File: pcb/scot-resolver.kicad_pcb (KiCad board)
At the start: 2 copper layers, 158 parts, among them IC1 AD8692ARMZ, IC10 AD2S1210, IC2 AD8397ARZ, IC3 AD8692ARMZ, IC4 TSR1, IC5 AD8692ARMZ, IC6 AD8692ARMZ, IC7 AD8692ARMZ, IC8 MCP2562, IC9 STM32F0xxKxTx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

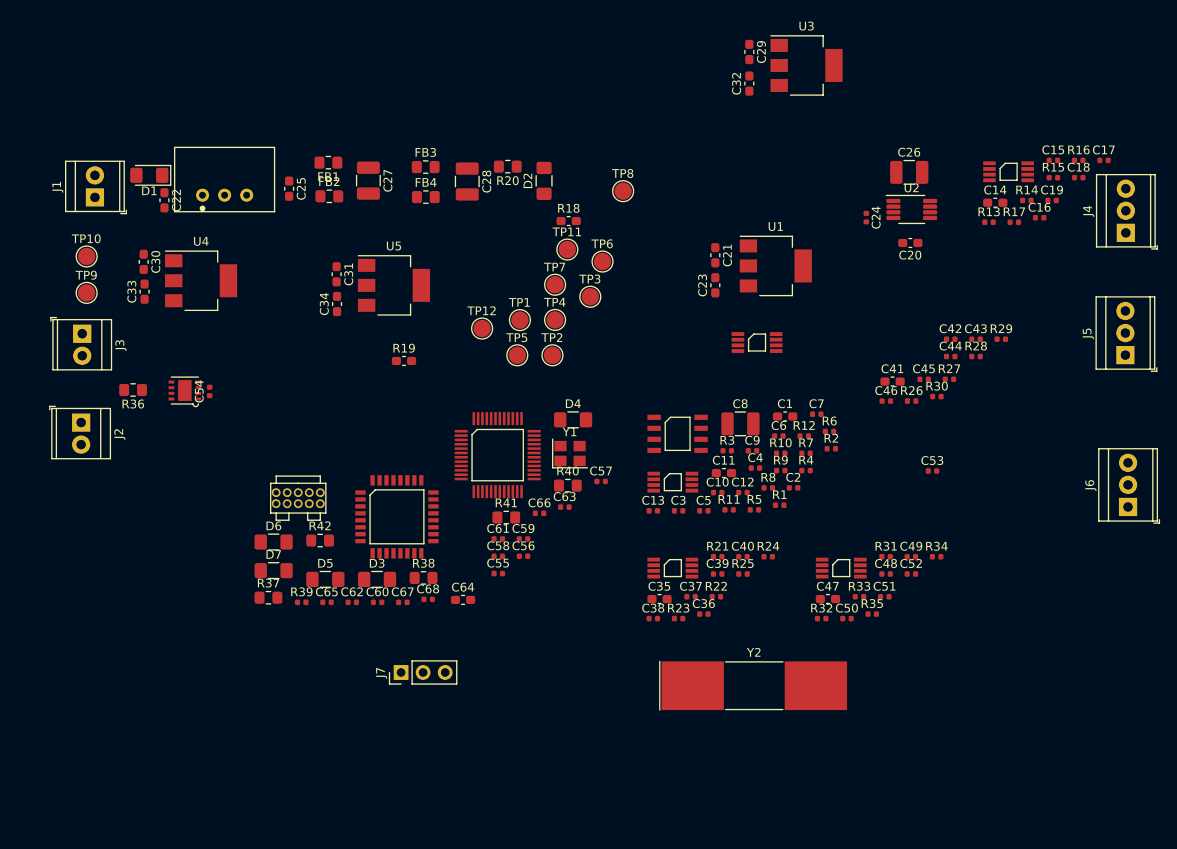
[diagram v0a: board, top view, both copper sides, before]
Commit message: PCB Progress, laying tracks.
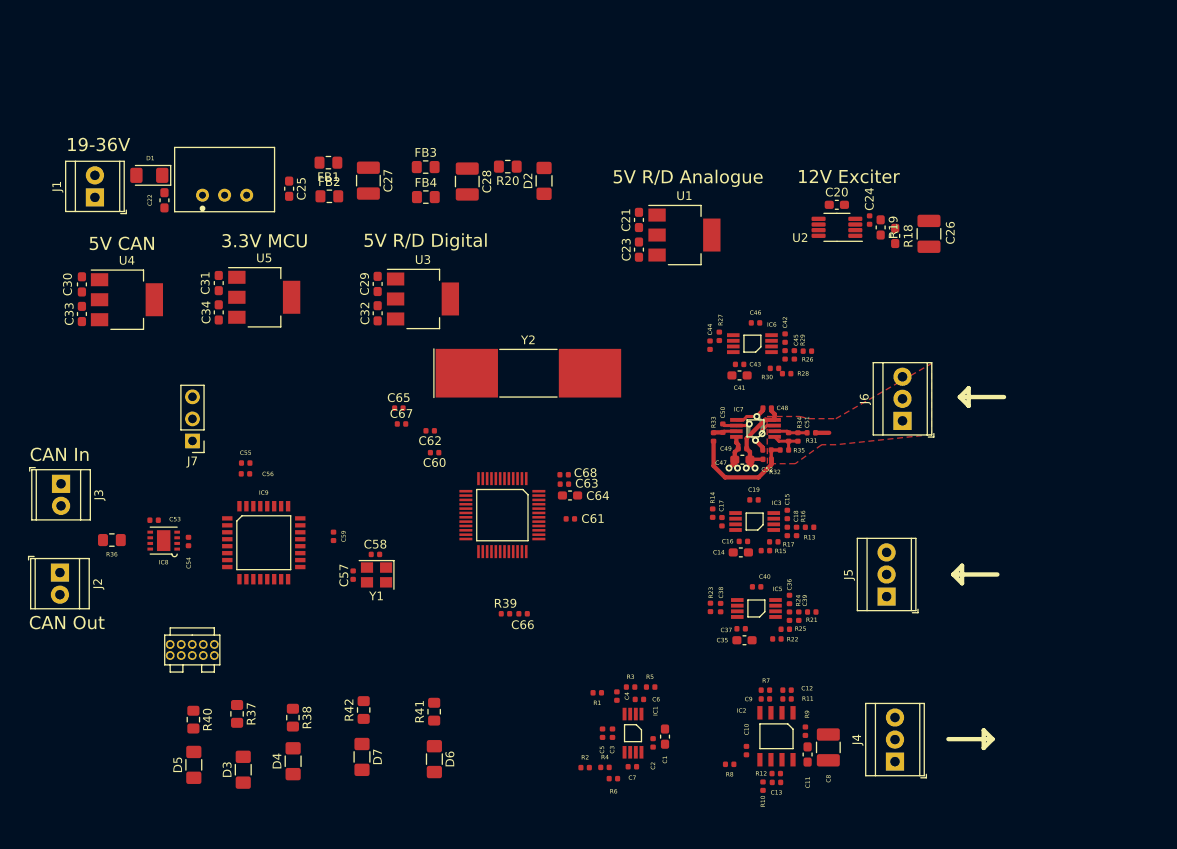
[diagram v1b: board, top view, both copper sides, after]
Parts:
- removed TP1, TP10, TP11, TP12, TP2, TP3, TP4, TP5, TP6, TP7, TP8, TP9: TestPoint, TestPoint:TestPoint_Pad_D2.0mm
- moved C53 89.8 mm to (92.8, 97.5), turned to 180 degrees
- moved J4 66.4 mm to (178.1, 125.3)
- moved C17 60.5 mm to (158.1, 97.7), turned to 270 degrees
- moved R19 57.0 mm to (176.4, 63.8), turned to 90 degrees
- moved R15 54.2 mm to (163.1, 101.0)
- moved R16 53.6 mm to (166.7, 98.8), turned to 270 degrees
- moved C18 52.7 mm to (165.7, 98.8), turned to 270 degrees
- moved U3 51.7 mm to (123.7, 72.1)
- moved R14 51.0 mm to (157.1, 96.7), turned to 90 degrees
- moved C15 51.0 mm to (165.7, 96.9), turned to 270 degrees
- moved R40 50.8 mm to (97.3, 120.5), turned to 270 degrees
- moved D4 50.8 mm to (108.8, 125.3), turned to 90 degrees
- moved C16 50.5 mm to (160.6, 100.0), turned to 180 degrees
- moved C29 50.4 mm to (118.5, 70.3)
- moved C32 50.3 mm to (118.5, 73.7)
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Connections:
- C12 pad 2: /Resolver Exciter/EXC+_OUTPUT -> /Resolver Exciter/EXC-_OUTPUT
- C13 pad 1: /Resolver Exciter/EXC-_OUTPUT -> /Resolver Exciter/EXC+_OUTPUT
- IC2 pad 1: /Resolver Exciter/EXC+_OUTPUT -> /Resolver Exciter/EXC-_OUTPUT
- IC2 pad 7: /Resolver Exciter/EXC-_OUTPUT -> /Resolver Exciter/EXC+_OUTPUT
- J4 pad 2: /Resolver Exciter/EXC-_OUTPUT -> /Resolver Exciter/EXC+_OUTPUT
- J4 pad 3: /Resolver Exciter/EXC+_OUTPUT -> /Resolver Exciter/EXC-_OUTPUT
- R1 pad 2: /Resolver Exciter/AD2S1210_EXC+ -> /Resolver Exciter/AD2S1210_EXC-
- R11 pad 2: /Resolver Exciter/EXC+_OUTPUT -> /Resolver Exciter/EXC-_OUTPUT
- R12 pad 1: /Resolver Exciter/EXC-_OUTPUT -> /Resolver Exciter/EXC+_OUTPUT
- R2 pad 1: /Resolver Exciter/AD2S1210_EXC- -> /Resolver Exciter/AD2S1210_EXC+
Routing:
- net Net-(C52-Pad1): track 0.00 -> 13.4 mm
- net GNDA: track 0.00 -> 12.1 mm, vias 0 -> 2
- net /Resolver Exciter/AD2S1210_VREF: track 0.00 -> 8.05 mm, vias 0 -> 2
- net Net-(C50-Pad1): track 0.00 -> 6.84 mm, vias 0 -> 2
- net /Microcontroller & Interface/5V_RESOLVER_ANALOGUE: track 0.00 -> 5.20 mm, vias 0 -> 2
- net Net-(C51-Pad2): track 0.00 -> 3.95 mm
- net Net-(C51-Pad1): track 0.00 -> 3.81 mm
- net /Resolver Receiver COS-/AD2S1210_INPUT: track 0.00 -> 2.70 mm
- net /Resolver Receiver COS-/RECEIVER_INPUT: track 0.00 -> 1.57 mm
- added copper zone on F.Cu, net GNDA
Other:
- board text added: "12V Exciter"
- board text added: "19-36V"
- board text added: "3.3V MCU"
- board text added: "5V CAN"
- board text added: "5V R/D Analogue"
- board text added: "5V R/D Digital"
- board text added: "CAN In"
- board text added: "CAN Out"

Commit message: Progress.
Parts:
- moved R28 9.07 mm to (156.8, 78.3), turned to 270 degrees
- moved R27 6.03 mm to (162.9, 79.6), turned to 0 degrees
- moved C46 5.90 mm to (163.0, 80.6), turned to 180 degrees
- moved C42 2.95 mm to (163.0, 74.8), turned to 180 degrees
- moved C44 1.10 mm to (157.9, 77.2)
- moved R30 0.88 mm to (164.9, 79.6), turned to 0 degrees
- moved C45 0.38 mm to (165.4, 78.1)
- moved R26 0.38 mm to (168.0, 77.7)
- moved R29 0.38 mm to (166.5, 78.1)
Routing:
- net Net-(C46-Pad1): track 0.00 -> 14.0 mm
- net GNDA: track 12.1 -> 24.7 mm, vias 2 -> 4
- net Net-(C44-Pad1): track 0.00 -> 6.55 mm, vias 0 -> 2
- net /Microcontroller & Interface/5V_RESOLVER_ANALOGUE: track 5.20 -> 10.9 mm, vias 2 -> 4
- net Net-(C45-Pad2): track 0.00 -> 3.83 mm
- net Net-(C45-Pad1): track 0.00 -> 3.71 mm
- net /Resolver Receiver COS+/AD2S1210_INPUT: track 0.00 -> 2.70 mm
- net /Resolver Exciter/AD2S1210_VREF: track 8.05 -> 9.92 mm, vias 2 -> 3

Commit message: Progress.
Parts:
- moved R14 7.09 mm to (163.3, 100.1), turned to 0 degrees
- moved R15 6.50 mm to (157.1, 98.7), turned to 270 degrees
- moved C19 6.09 mm to (163.3, 101.1), turned to 180 degrees
- moved C40 6.07 mm to (163.5, 111.1), turned to 180 degrees
- moved R10 5.50 mm to (161.0, 123.0), turned to 90 degrees
- moved C15 2.86 mm to (163.2, 95.4), turned to 180 degrees
- moved C36 2.78 mm to (163.4, 105.4), turned to 180 degrees
- moved R22 1.51 mm to (163.4, 110.1)
- moved R23 1.26 mm to (157.4, 108.7), turned to 270 degrees
- moved R17 1.14 mm to (165.2, 100.1)
- moved C10 0.94 mm to (160.0, 124.1)
- moved C1 0.75 mm to (151.5, 123.2)
- moved R8 0.49 mm to (159.5, 125.6)
- moved C37 0.46 mm to (160.8, 110.0)
- moved C38 0.40 mm to (158.4, 107.7)
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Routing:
- net GNDA: track 24.7 -> 50.3 mm
- net /Resolver Exciter/AD2S1210_VREF: track 9.92 -> 32.7 mm, vias 3 -> 8
- net Net-(C38-Pad1): track 0.00 -> 7.02 mm, vias 0 -> 2
- net Net-(C17-Pad1): track 0.00 -> 6.79 mm, vias 0 -> 2
- net Net-(C12-Pad1): track 0.00 -> 6.76 mm
- net Net-(C13-Pad2): track 0.00 -> 6.46 mm
- net /Microcontroller & Interface/5V_RESOLVER_ANALOGUE: track 10.9 -> 16.9 mm
- net /Power Supplies/12V_EXCITER: track 0.00 -> 4.26 mm
- net Net-(C39-Pad2): track 0.00 -> 3.93 mm
- net Net-(C18-Pad2): track 0.00 -> 3.84 mm
- net Net-(C10-Pad2): track 0.00 -> 3.74 mm
- net Net-(C39-Pad1): track 0.00 -> 3.71 mm
- net Net-(C18-Pad1): track 0.00 -> 3.67 mm
- net /Resolver Exciter/EXC-_OUTPUT: track 0.00 -> 2.69 mm
- net /Resolver Exciter/EXC+_OUTPUT: track 0.00 -> 2.69 mm
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
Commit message: Progress.
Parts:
- moved D3 20.5 mm to (123.4, 124.6)
- moved D4 20.3 mm to (129.1, 124.3)
- moved D5 20.3 mm to (117.7, 124.7)
- moved R37 20.3 mm to (122.7, 118.8)
- moved R38 20.3 mm to (129.1, 119.2)
- moved R40 20.3 mm to (117.6, 119.5)
- moved D6 16.4 mm to (108.7, 125.3)
- moved R42 16.4 mm to (100.5, 119.6)
- moved D7 16.4 mm to (100.3, 125.0)
- moved R41 16.4 mm to (108.6, 119.8)
- moved C27 3.23 mm to (115.4, 60.9)
- moved FB2 2.50 mm to (111.7, 62.4)
- moved C5 2.25 mm to (144.5, 124.3)
- moved R1 1.85 mm to (145.6, 117.2)
- moved R2 1.60 mm to (144.0, 125.8)
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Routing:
- net /Power Supplies/POWER_28V-: track 0.00 -> 26.9 mm
- net GNDA: track 50.3 -> 69.4 mm, vias 4 -> 8
- net Net-(C40-Pad1): track 2.08 -> 14.0 mm
- net Net-(C19-Pad1): track 1.98 -> 13.5 mm
- net Net-(C25-Pad1): track 0.00 -> 8.46 mm
- net /Microcontroller & Interface/5V_RESOLVER_ANALOGUE: track 16.9 -> 25.3 mm, vias 4 -> 8
- net Net-(C22-Pad1): track 0.00 -> 7.52 mm
- net /Resolver Exciter/AD2S1210_VREF: track 32.7 -> 39.5 mm, vias 8 -> 10
- net Net-(C4-Pad1): track 0.00 -> 5.42 mm
- net /Power Supplies/POWER_28V+: track 0.00 -> 4.84 mm
- net Net-(C5-Pad2): track 0.00 -> 3.69 mm
- net AVCC: track 0.00 -> 3.28 mm
- net Net-(C7-Pad2): track 0.00 -> 3.26 mm
- net Net-(C6-Pad2): track 0.00 -> 2.73 mm
- net Net-(C7-Pad1): track 0.00 -> 2.60 mm
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
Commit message: Progress.
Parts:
- moved C26 37.8 mm to (144.8, 71.1), turned to 180 degrees
- moved R18 30.1 mm to (148.6, 70.8)
- moved C20 28.1 mm to (143.5, 65.1)
- moved U2 28.1 mm to (143.6, 67.7)
- moved C24 28.1 mm to (147.3, 66.8)
- moved R19 28.0 mm to (148.6, 67.5)
- moved C67 28.0 mm to (148.6, 80.6)
- moved C21 8.04 mm to (155.8, 66.5)
- moved C23 8.04 mm to (155.8, 69.9)
- moved U1 8.04 mm to (161.1, 68.2)
- moved C65 4.75 mm to (123.3, 80.5), turned to 180 degrees
- moved J6 4.36 mm to (174.6, 86.2)
- moved C10 2.58 mm to (157.5, 123.7)
- moved C13 2.58 mm to (161.9, 127.3)
- moved C8 2.58 mm to (167.8, 123.2)
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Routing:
- net /Power Supplies/12V_EXCITER: track 4.26 -> 15.4 mm, vias 0 -> 2
- net GNDA: track 69.4 -> 80.4 mm
- net /Resolver Exciter/EXC+_OUTPUT: track 2.69 -> 10.3 mm
- net /Resolver Receiver COS+/RECEIVER_INPUT: track 0.00 -> 7.24 mm
- net AVCC: track 3.28 -> 9.53 mm
- net /Resolver Exciter/EXC-_OUTPUT: track 2.69 -> 8.68 mm
- net /Resolver Receiver COS-/RECEIVER_INPUT: track 1.57 -> 7.25 mm
- net Net-(R18-Pad2): track 0.00 -> 4.66 mm
- net /Microcontroller & Interface/5V_RESOLVER_ANALOGUE: track 25.3 -> 28.6 mm, vias 8 -> 10
- net Net-(C24-Pad1): track 0.00 -> 1.70 mm

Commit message: WIP.
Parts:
- moved D2 8.73 mm to (129.3, 60.9)
- moved R20 7.77 mm to (126.2, 59.4)
- moved C28 6.71 mm to (122.6, 60.9)
- moved FB4 5.48 mm to (119.0, 62.4)
- moved FB3 5.15 mm to (118.9, 57.5)
- moved FB1 0.25 mm to (111.7, 56.4)
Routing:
- net GND: track 0.00 -> 14.4 mm
- net +15V: track 0.00 -> 6.53 mm
- net Net-(C25-Pad1): track 8.46 -> 4.93 mm
- net AVCC: track 9.53 -> 6.26 mm
- net GNDA: track 80.4 -> 83.0 mm
- net /CAN TXRX/3.3V_MCU: track 0.00 -> 2.21 mm
- net /Microcontroller & Interface/5V_RESOLVER_DIGITAL: track 0.00 -> 2.16 mm
- net /CAN TXRX/5V_CAN: track 0.00 -> 2.12 mm
- net Net-(C22-Pad1): track 7.52 -> 6.16 mm
- net /Power Supplies/POWER_28V-: track 26.9 -> 28.1 mm
- added copper zone on F.Cu, net GND

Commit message: WIP
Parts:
- moved C26 35.8 mm to (179.9, 64.0), turned to 270 degrees
- moved U2 33.0 mm to (176.5, 65.2), turned to 270 degrees
- moved R18 32.8 mm to (179.6, 60.2), turned to 180 degrees
- moved C20 30.3 mm to (173.9, 65.2), turned to 90 degrees
- moved C24 28.7 mm to (175.5, 61.5), turned to 180 degrees
- moved R19 28.6 mm to (176.2, 60.2), turned to 180 degrees
- moved Y1 26.0 mm to (106.3, 80.9), turned to 0 degrees
- moved C57 23.3 mm to (109.0, 81.6), turned to 90 degrees
- moved C58 21.3 mm to (107.4, 83.1), turned to 0 degrees
- moved J7 20.0 mm to (102.7, 107.7), turned to 270 degrees
- moved C59 16.2 mm to (105.7, 85.2), turned to 90 degrees
- moved P1 15.9 mm to (111.9, 106.3)
- moved C35 11.8 mm to (166.1, 100.9)
- moved C39 11.8 mm to (172.3, 98.0)
- moved C40 11.8 mm to (168.8, 100.6)
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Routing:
- net GNDA: track 83.0 -> 337.7 mm, vias 8 -> 21
- net GND: track 14.4 -> 139.4 mm, vias 0 -> 5
- net /Microcontroller & Interface/5V_RESOLVER_ANALOGUE: track 28.6 -> 129.1 mm, vias 10 -> 11
- net /CAN TXRX/3.3V_MCU: track 2.21 -> 96.1 mm, vias 0 -> 4
- net AVCC: track 6.26 -> 92.8 mm, vias 0 -> 3
- net /Power Supplies/12V_EXCITER: track 15.4 -> 100.8 mm, vias 2 -> 3
- net +15V: track 6.53 -> 59.7 mm
- net /Resolver Exciter/AD2S1210_EXC+: track 0.00 -> 33.0 mm
- net /Resolver Receiver SIN+/AD2S1210_INPUT: track 2.67 -> 34.0 mm
- net /Resolver Receiver SIN-/AD2S1210_INPUT: track 2.64 -> 32.5 mm
- net /Resolver Receiver COS-/AD2S1210_INPUT: track 2.70 -> 32.6 mm
- net /Resolver Receiver COS+/AD2S1210_INPUT: track 2.70 -> 32.5 mm
- net /Resolver Exciter/AD2S1210_EXC-: track 0.00 -> 26.7 mm
- net /CAN TXRX/5V_CAN: track 2.12 -> 27.7 mm, vias 0 -> 2
- net /CAN TXRX/CAN_L: track 0.00 -> 23.7 mm, vias 0 -> 1
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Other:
- board text added: "15V OK"

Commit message: WIP.
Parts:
- moved R37 11.8 mm to (134.4, 118.2)
- moved D3 11.8 mm to (135.2, 124.0)
- moved U1 11.0 mm to (151.3, 60.1)
- moved C21 11.0 mm to (146.1, 58.3)
- moved C23 11.0 mm to (146.1, 61.8)
- moved R40 9.98 mm to (127.6, 119.0)
- moved D5 9.98 mm to (127.6, 124.2)
- moved D4 8.54 mm to (120.6, 125.0)
- moved R38 8.54 mm to (120.6, 120.0)
- moved J7 6.36 mm to (96.4, 106.6)
- moved C66 3.66 mm to (135.8, 104.7)
- moved R39 3.66 mm to (133.8, 104.7)
- moved R18 3.59 mm to (177.1, 57.7)
- moved C20 3.59 mm to (171.3, 62.7)
- moved C24 3.59 mm to (173.0, 58.9)
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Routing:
- net /Microcontroller & Interface/~LOT: track 14.0 -> 65.5 mm, vias 1 -> 4
- net GND: track 139.4 -> 187.5 mm, vias 5 -> 7
- net /CAN TXRX/3.3V_MCU: track 96.1 -> 139.9 mm, vias 4 -> 9
- net GNDA: track 337.7 -> 377.8 mm, vias 21 -> 83
- net /Microcontroller & Interface/5V_RESOLVER_ANALOGUE: track 129.1 -> 161.3 mm
- net /Microcontroller & Interface/A0: track 14.1 -> 42.6 mm, vias 1 -> 2
- net /Microcontroller & Interface/RES0: track 15.0 -> 43.3 mm, vias 1 -> 2
- net /Microcontroller & Interface/A1: track 14.0 -> 39.3 mm, vias 1 -> 4
- net /Microcontroller & Interface/RES1: track 14.4 -> 39.0 mm, vias 1 -> 2
- net /Microcontroller & Interface/~DOT: track 14.0 -> 38.4 mm, vias 1 -> 4
- net /Microcontroller & Interface/~SAMPLE: track 15.8 -> 35.4 mm, vias 1 -> 2
- net /Microcontroller & Interface/SPI_RD_~CS: track 6.19 -> 25.6 mm, vias 0 -> 2
- net /Microcontroller & Interface/SPI_RD_MISO: track 6.13 -> 22.3 mm, vias 0 -> 2
- net /Microcontroller & Interface/SPI_RD_MOSI: track 6.17 -> 20.6 mm
- net Net-(C65-Pad1): track 6.04 -> 19.6 mm
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- added copper zone on B.Cu, net GNDA
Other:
- board text added: "Degradation"
- board text added: "INC-A"
- board text added: "INC-B"
- board text added: "INC-NM"
- board text added: "Loss"
- board text added: "SWD"
- board text added: "UART"
